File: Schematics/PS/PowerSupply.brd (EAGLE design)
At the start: 157.5 x 127 mm, 79 parts, among them IC1 LM317MABDT, IC2 LM337, T1 IRFP240, T2 IRFP240

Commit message: updates to PS
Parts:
- moved C3 144.5 mm to (144.1, 12.6)
- moved D11 94.0 mm to (170.2, 17.6)
- moved D18 68.4 mm to (126.6, 12.2)
- moved C21 58.1 mm to (144.8, 35.0), turned to 270 degrees
- moved C24 55.6 mm to (163.3, 56.4)
- moved IC2 48.8 mm to (152.4, 24.5)
- moved C18 47.1 mm to (137.9, 37.9), turned to 270 degrees
- moved C22 46.6 mm to (152.9, 34.8)
- moved R12 45.6 mm to (153.5, 55.8), turned to 90 degrees
- moved C8 44.0 mm to (79.9, 13.5)
- moved R21 41.5 mm to (187.2, 51.3)
- moved IC1 35.6 mm to (137.8, 23.6), turned to 180 degrees
- moved C20 29.6 mm to (148.7, 41.5), turned to 180 degrees
- moved D14 25.1 mm to (137.8, 46.1), turned to 90 degrees
- moved D17 24.8 mm to (153.2, 19.3)
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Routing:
- net MUTE: track 4.44 -> 62.0 mm
- net V+: track 128.5 -> 91.1 mm
- net N$10: track 15.6 -> 48.6 mm
- net SGND: track 54.5 -> 84.0 mm
- net VAC+15: track 0.00 -> 23.3 mm
- net VAC-15: track 0.00 -> 17.8 mm
- net N$1: track 17.4 -> 23.2 mm
- net N$21: track 9.27 -> 14.7 mm
- net VAC+40: track 50.0 -> 55.1 mm
- net VAC-40: track 34.9 -> 39.8 mm
- net V-15UN: track 0.00 -> 3.07 mm
- net V15UN: track 0.00 -> 2.74 mm
- net N$9: track 32.1 -> 34.8 mm
- net N$22: track 91.1 -> 93.7 mm
- net VCC: track 119.0 -> 120.2 mm
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
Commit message: finished powersuply :) updated parts on hand
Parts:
- C28: device rcl:C102-064X133 -> rcl:C0805K
- moved R21 125.2 mm to (62.9, 35.7), turned to 180 degrees
- moved C23 118.8 mm to (76.2, 26.6), turned to 90 degrees
- moved R22 118.5 mm to (61.3, 31.0), turned to 90 degrees
- moved C24 109.8 mm to (57.1, 28.3), turned to 90 degrees
- moved D17 89.6 mm to (64.7, 33.8), turned to 270 degrees
- moved D12 80.6 mm to (147.6, 20.9), turned to 90 degrees
- moved IC2 79.8 mm to (73.2, 33.8), turned to 270 degrees
- moved C3 76.0 mm to (69.1, 24.6), turned to 90 degrees
- moved R19 73.7 mm to (147.0, 19.7)
- moved C8 71.7 mm to (29.8, 64.9), turned to 180 degrees
- moved C6 69.6 mm to (143.1, 22.4), turned to 180 degrees
- moved C14 67.3 mm to (152.0, 20.8)
- moved D18 61.3 mm to (67.6, 29.0)
- moved C16 40.6 mm to (150.4, 29.0), turned to 90 degrees
- moved R18 32.8 mm to (16.2, 60.4), turned to 90 degrees
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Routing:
- net V15+: track 0.00 -> 130.5 mm
- net VEE: track 44.8 -> 169.4 mm
- net MUTE: track 62.0 -> 182.6 mm
- net V-15UN: track 3.07 -> 122.5 mm
- net VCC: track 120.2 -> 197.2 mm
- net V15-: track 0.00 -> 36.2 mm
- net V15UN: track 2.74 -> 36.7 mm
- net N$3: track 0.00 -> 18.9 mm
- net GND: track 11.2 -> 28.7 mm, vias 0 -> 1
- net N$26: track 0.00 -> 13.7 mm
- net EGND: track 27.0 -> 31.1 mm
- net N$25: track 0.00 -> 3.82 mm
- net N$8: track 0.00 -> 2.88 mm
- net VAC+40: track 55.1 -> 56.4 mm
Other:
- board size 157.5 x 127 mm -> 157.5 x 109.9 mm

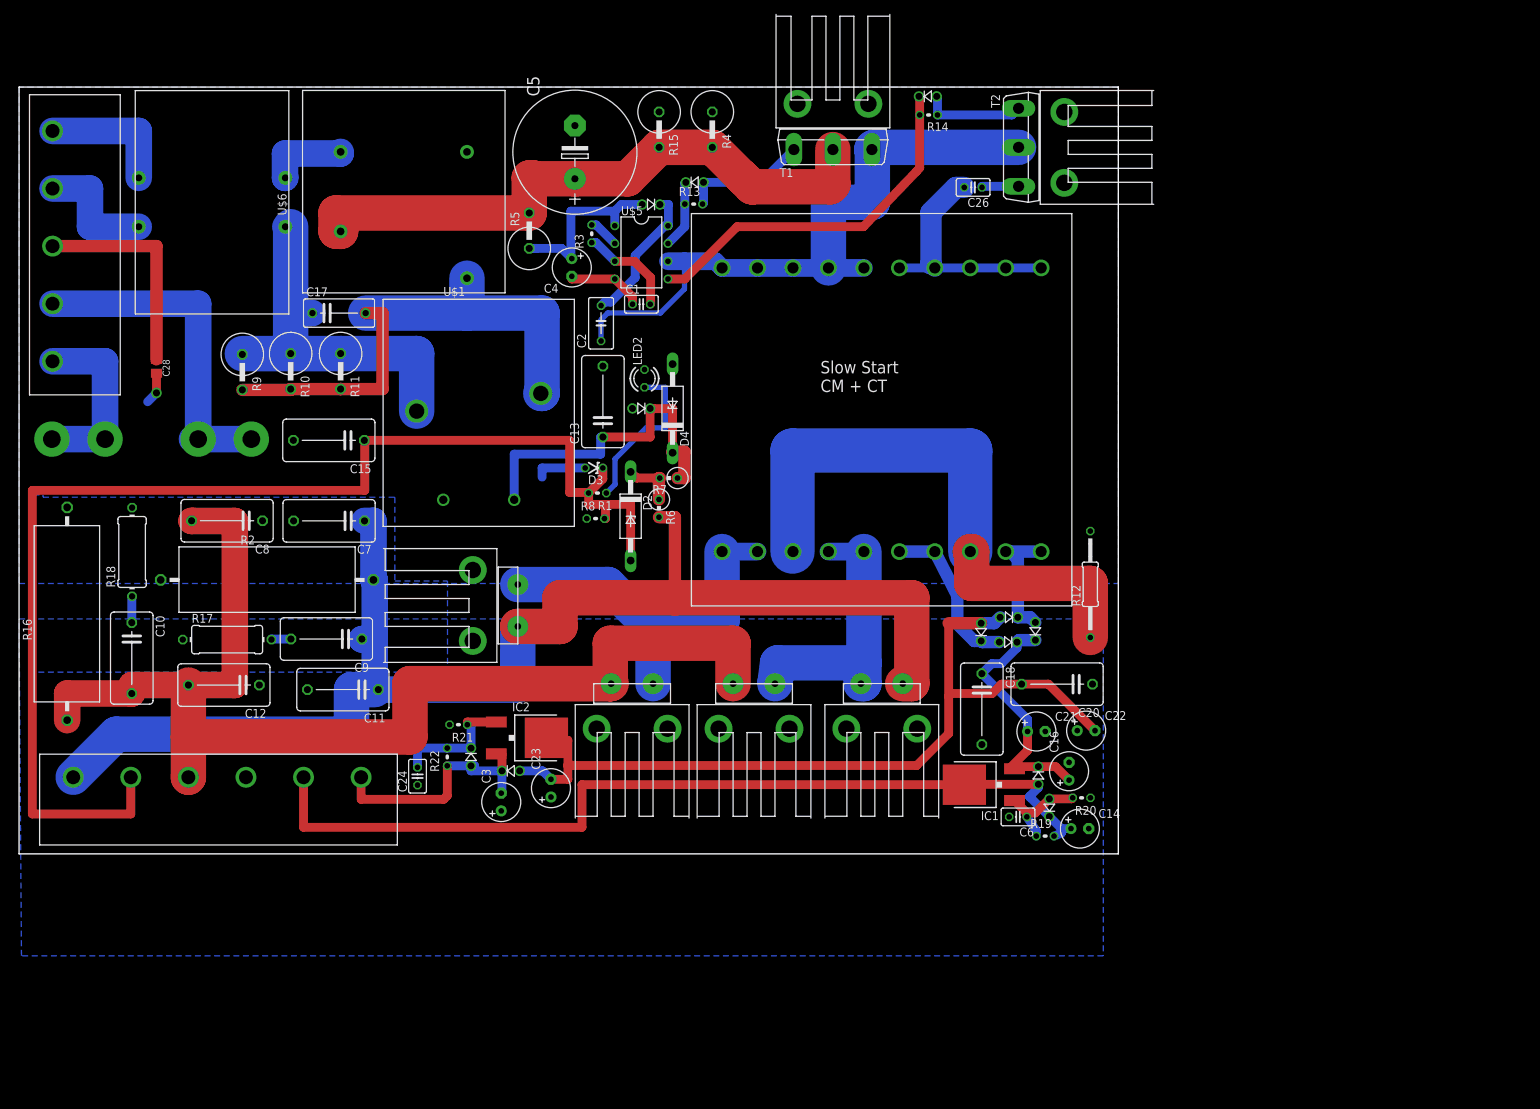
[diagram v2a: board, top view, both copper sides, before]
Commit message: fixed PS layout (changed rectifier footprint)
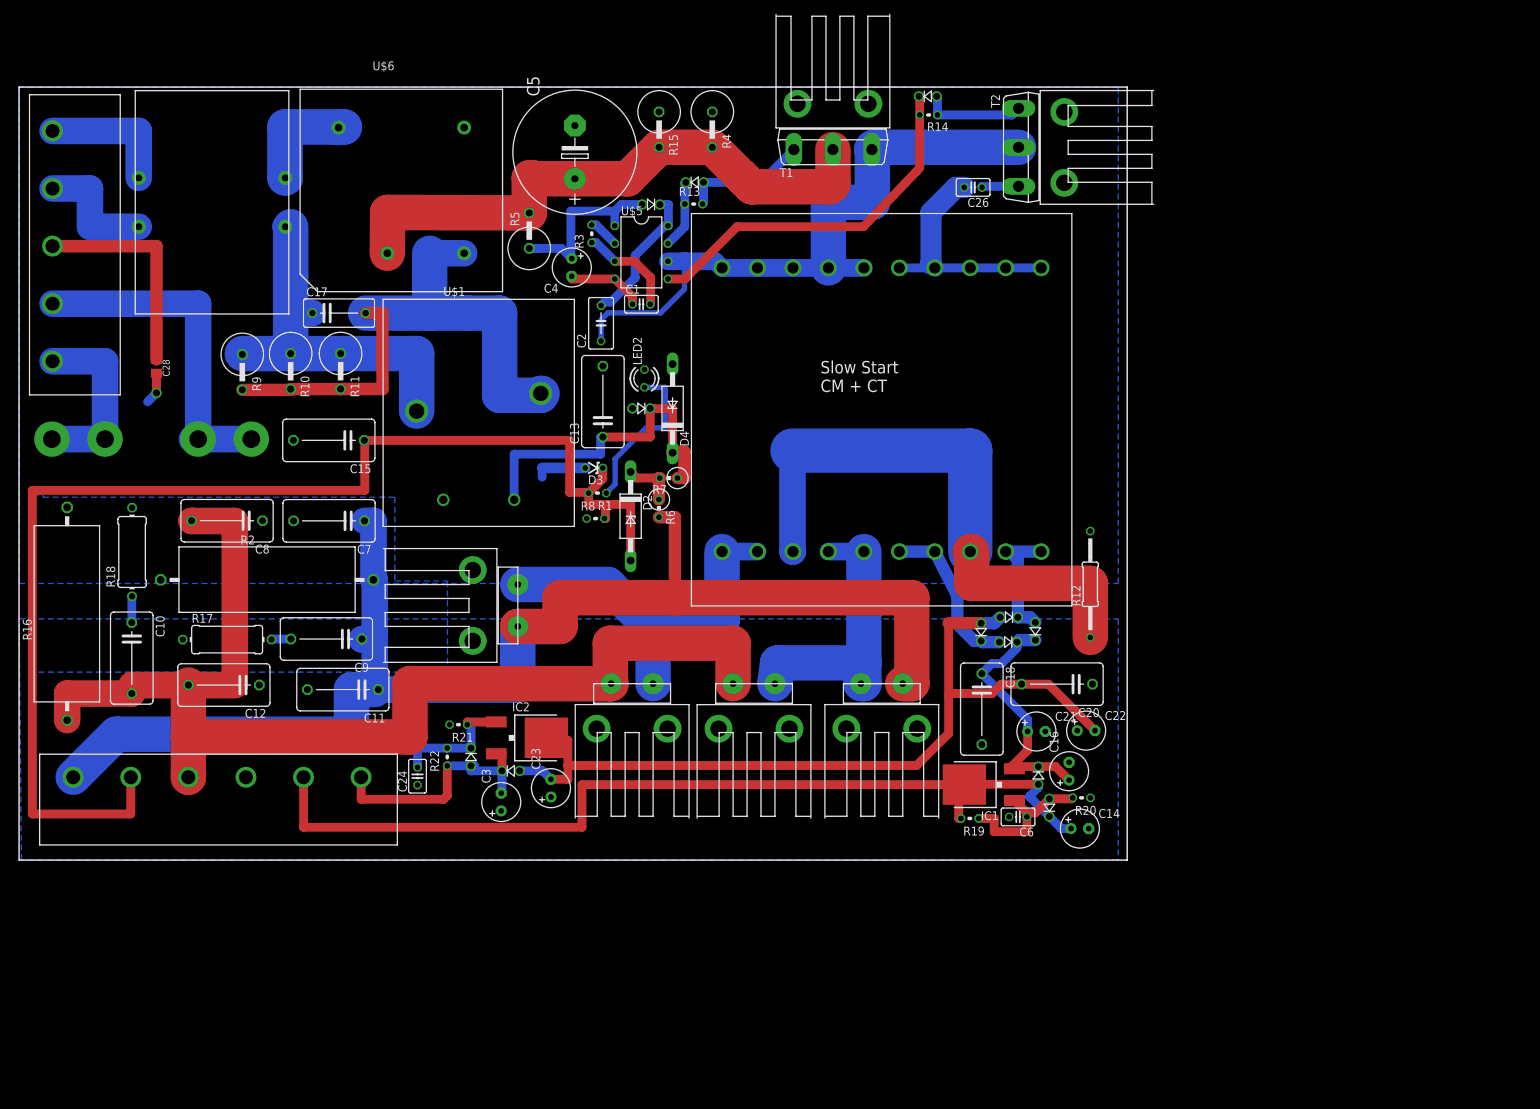
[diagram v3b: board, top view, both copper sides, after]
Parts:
- moved R19 11.1 mm to (136.2, 22.2), turned to 180 degrees
- moved U$6 8.03 mm to (52.8, 103.2), turned to 0 degrees
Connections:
- net GND: now also U$6.-; no longer U$6.V-
- net V+: now also U$6.+; no longer U$6.V+
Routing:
- net N$18: track 75.5 -> 84.4 mm
- net N$26: track 13.7 -> 21.5 mm
- net N$4: track 11.7 -> 16.7 mm
- net V+: track 91.1 -> 86.3 mm
- net V15+: track 130.5 -> 133.9 mm
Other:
- board size 157.5 x 109.9 mm -> 158.8 x 110.7 mm
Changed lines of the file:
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@@
 <setting verticaltext="up"/>
 </settings>
-<grid distance="0.025" unitdist="inch" unit="inch" style="lines" multiple="1" display="yes" altdistance="0.025" altunitdist="inch" altunit="inch"/>
+<grid distance="0.003125" unitdist="mic" unit="inch" style="lines" multiple="1" display="yes" altdistance="0.025" altunitdist="inch" altunit="inch"/>
 <layers>
 <layer number="1" name="Top" color="4" fill="1" visible="yes" active="yes"/>
@@
 <board>
 <plain>
-<wire x1="0" y1="17.145" x2="157.48" y2="17.145" width="0" layer="20"/>
-<wire x1="157.48" y1="17.145" x2="157.48" y2="127" width="0" layer="20"/>
-<wire x1="157.48" y1="127" x2="0" y2="127" width="0" layer="20"/>
-<wire x1="0" y1="127" x2="0" y2="17.145" width="0" layer="20"/>
+<wire x1="0" y1="16.256" x2="158.75" y2="16.256" width="0" layer="20"/>
+<wire x1="158.75" y1="16.256" x2="158.75" y2="127" width="0" layer="20"/>
+<wire x1="158.75" y1="127" x2="0" y2="127" width="0" layer="20"/>
+<wire x1="0" y1="127" x2="0" y2="16.256" width="0" layer="20"/>
 <text x="114.808" y="83.312" size="1.778" layer="21" font="vector">Slow Start
 CM + CT</text>
@@
 <element name="R3" library="rcl" package="0204V" value="" x="82.042" y="105.9815" rot="R90"/>
 <element name="C1" library="resistor" package="C025-025X050" value="" x="89.154" y="95.885"/>
-<element name="U$6" library="Amplifier_Parts" package="GBPC3510W" value="GBPC3510W" x="50.038" y="110.744" rot="R90"/>
+<element name="U$6" library="Amplifier_Parts" package="GBPC3510W" value="GBPC3510W" x="52.76455625" y="103.188453125"/>
 <element name="C4" library="rcl" package="E2,5-6" value="100uF" x="79.1845" y="101.1555" smashed="yes" rot="R270">
 <attribute name="NAME" x="75.184" y="97.536" size="1.27" layer="25" ratio="10"/>
@@
 <element name="D11" library="Amplifier_Parts" package="1N4004" value="1N4004" x="146.0256875" y="31.1901875" rot="R270"/>
 <element name="D12" library="Amplifier_Parts" package="1N4004" value="1N4004" x="147.60016875" y="20.948165625" rot="R90"/>
-<element name="R19" library="rcl" package="0204V" value="10k" x="147.000615625" y="19.693478125"/>
+<element name="R19" library="rcl" package="0204V" value="10k" x="136.209384375" y="22.216521875" rot="R180"/>
 <element name="R20" library="rcl" package="0204V" value="10k" x="152.216559375" y="25.17390625" rot="R180"/>
 <element name="C6" library="resistor" package="C025-025X050" value="10uF" x="143.111490625" y="22.441559375" rot="R180"/>
@@
 <contactref element="C26" pad="1"/>
 <contactref element="C28" pad="2"/>
-<contactref element="U$6" pad="V-"/>
+<contactref element="U$6" pad="-"/>
 <contactref element="C5" pad="-"/>
 <contactref element="R15" pad="1"/>
@@
 <wire x1="143.1925" y1="112.776" x2="137.9474" y2="112.776" width="1.27" layer="16"/>
 <wire x1="137.9474" y1="112.776" x2="137.9474" y2="112.6236" width="1.27" layer="16"/>
-<wire x1="81.0934375" y1="72.432103125" x2="74.93" y2="72.432103125" width="1.27" layer="16"/>
+<wire x1="81.0934375" y1="72.432103125" x2="74.93" y2="72.432103125" width="1.524" layer="16"/>
 <wire x1="74.93" y1="72.432103125" x2="74.93" y2="71.12" width="1.27" layer="16"/>
 </signal>
@@
 <signal name="V+">
 <contactref element="T1" pad="D"/>
-<contactref element="U$6" pad="V+"/>
+<contactref element="U$6" pad="+"/>
 <contactref element="C5" pad="+"/>
 <contactref element="R15" pad="2"/>
@@
 <wire x1="73.66" y1="113.9825" x2="73.0885" y2="113.9825" width="5.08" layer="1"/>
 <wire x1="73.0885" y1="113.9825" x2="73.0885" y2="108.966" width="5.08" layer="1"/>
-<wire x1="73.0885" y1="108.966" x2="45.4025" y2="108.966" width="5.08" layer="1"/>
-<wire x1="45.4025" y1="108.966" x2="45.4025" y2="106.3625" width="5.08" layer="1"/>
-<wire x1="45.4025" y1="106.3625" x2="46.068" y2="106.3625" width="5.08" layer="1"/>
-<wire x1="46.068" y1="106.3625" x2="46.068" y2="106.314" width="5.08" layer="1"/>
+<wire x1="73.0885" y1="108.966" x2="52.7991" y2="109.0407" width="5.08" layer="1"/>
+<wire x1="52.7991" y1="109.0407" x2="52.76455625" y2="103.188453125" width="5.08" layer="1"/>
 </signal>
 <signal name="N$17">
@@
 <contactref element="C17" pad="2"/>
 <contactref element="U$6" pad="AC2"/>
-<wire x1="49.6514" y1="94.61909375" x2="64.168" y2="94.61909375" width="5.08" layer="16"/>
-<wire x1="64.168" y1="94.61909375" x2="64.168" y2="99.614" width="5.08" layer="16"/>
+<wire x1="49.6514" y1="94.61909375" x2="58.8267" y2="94.61909375" width="5.08" layer="16"/>
+<wire x1="58.8267" y1="94.61909375" x2="64.168" y2="94.61909375" width="5.08" layer="16"/>
 <wire x1="74.741696875" y1="83.110078125" x2="74.93" y2="83.110078125" width="5.08" layer="16"/>
-<wire x1="74.93" y1="83.110078125" x2="74.93" y2="94.615" width="5.08" layer="16"/>
-<wire x1="74.93" y1="94.615" x2="64.168" y2="94.615" width="5.08" layer="16"/>
 <wire x1="64.168" y1="94.615" x2="64.168" y2="94.61909375" width="5.08" layer="16"/>
 <wire x1="31.983978125" y1="83.615234375" x2="38.907159375" y2="83.615234375" width="1.778" layer="1"/>
@@
 <wire x1="52.07" y1="83.741671875" x2="52.07" y2="94.61909375" width="1.778" layer="1"/>
 <wire x1="52.07" y1="94.61909375" x2="49.6514" y2="94.61909375" width="1.778" layer="1"/>
+<wire x1="63.76455625" y1="103.188453125" x2="58.8267" y2="103.188453125" width="3.81" layer="16"/>
+<wire x1="58.8267" y1="103.188453125" x2="58.8267" y2="94.61909375" width="5.08" layer="16"/>
+<wire x1="64.168" y1="94.615" x2="68.843828125" y2="94.615" width="5.08" layer="16"/>
+<wire x1="68.843828125" y1="94.615" x2="68.843828125" y2="82.834596875" width="5.08" layer="16"/>
+<wire x1="68.843828125" y1="82.834596875" x2="74.741696875" y2="82.834596875" width="5.08" layer="16"/>
+<wire x1="74.741696875" y1="82.834596875" x2="74.741696875" y2="83.110078125" width="5.08" layer="16"/>
 </signal>
 <signal name="N$1">
@@
 <contactref element="U$3" pad="P$3"/>
 <contactref element="C14" pad="-"/>
-<wire x1="110.871" y1="60.452" x2="110.8075" y2="60.452" width="5.08" layer="16"/>
-<wire x1="110.8075" y1="60.452" x2="110.8075" y2="74.93" width="6.35" layer="16"/>
+<wire x1="110.871" y1="60.452" x2="110.8075" y2="60.452" width="3.81" layer="16"/>
+<wire x1="110.8075" y1="60.452" x2="110.8075" y2="74.93" width="3.81" layer="16"/>
 <wire x1="110.8075" y1="74.93" x2="136.271" y2="74.93" width="6.35" layer="16"/>
 <wire x1="136.271" y1="74.93" x2="136.271" y2="60.452" width="6.35" layer="16"/>
 <contactref element="C3" pad="+"/>
-<polygon width="0.254" layer="16" isolate="0.762">
+<polygon width="0.254" layer="16" isolate="1.27">
 <vertex x="0" y="50.8"/>
-<vertex x="155.3337" y="50.8"/>
-<vertex x="155.3337" y="2.54"/>
-<vertex x="0.3429" y="2.54"/>
+<vertex x="157.48" y="50.8"/>
+<vertex x="157.48" y="16.256"/>
+<vertex x="0.3429" y="16.256"/>
 </polygon>
 <polygon width="0.254" layer="16" isolate="2.032">
@@
 <wire x1="147.60016875" y1="22.488165625" x2="149.320571875" y2="20.7677625" width="1.27" layer="16"/>
 <wire x1="149.320571875" y1="20.7677625" x2="150.700871875" y2="20.7677625" width="1.27" layer="16"/>
-<wire x1="148.270615625" y1="19.693478125" x2="149.320571875" y2="20.108434375" width="1.27" layer="16"/>
-<wire x1="149.320571875" y1="20.108434375" x2="149.320571875" y2="20.7677625" width="1.27" layer="16"/>
-<wire x1="135.429659375" y1="27.06104375" x2="80.645" y2="27.06104375" width="1.27" layer="1"/>
+<wire x1="135.429659375" y1="27.06104375" x2="134.62" y2="27.06104375" width="1.27" layer="1"/>
+<wire x1="134.62" y1="27.06104375" x2="80.645" y2="27.06104375" width="1.27" layer="1"/>
 <wire x1="80.645" y1="27.06104375" x2="80.645" y2="20.955" width="1.27" layer="1"/>
 <wire x1="80.645" y1="20.955" x2="40.754225" y2="20.955" width="1.27" layer="1"/>
@@
 <wire x1="144.78" y1="25.4" x2="144.78" y2="25.308334375" width="1.27" layer="16"/>
 <wire x1="144.78" y1="25.308334375" x2="147.60016875" y2="22.488165625" width="1.27" layer="16"/>
+<wire x1="134.939384375" y1="22.216521875" x2="134.62" y2="22.216521875" width="1.27" layer="1"/>
+<wire x1="134.62" y1="22.216521875" x2="134.62" y2="27.06104375" width="1.27" layer="1"/>
 </signal>
 <signal name="N$26">
@@
 <wire x1="150.946559375" y1="25.17390625" x2="150.80081875" y2="25.028165625" width="1.27" layer="1"/>
 <wire x1="150.80081875" y1="25.028165625" x2="147.60016875" y2="25.028165625" width="1.27" layer="1"/>
-<wire x1="144.381490625" y1="22.441559375" x2="145.730615625" y2="20.457434375" width="1.27" layer="16"/>
-<wire x1="145.730615625" y1="20.457434375" x2="145.730615625" y2="19.693478125" width="1.27" layer="16"/>
+<wire x1="137.479384375" y1="22.216521875" x2="139.7" y2="22.216521875" width="1.27" layer="1"/>
+<wire x1="139.7" y1="22.216521875" x2="139.7" y2="20.32" width="1.27" layer="1"/>
+<wire x1="139.7" y1="20.32" x2="144.381490625" y2="20.32" width="1.27" layer="1"/>
+<wire x1="144.381490625" y1="20.32" x2="144.381490625" y2="22.441559375" width="1.27" layer="1"/>
 </signal>
 <signal name="V15UN">
@@
 <contactref element="U$6" pad="AC1"/>
 <contactref element="L2" pad="PASS2"/>
-<wire x1="38.145" y1="113.99" x2="38.1" y2="113.99" width="3.81" layer="16"/>
-<wire x1="38.1" y1="113.99" x2="38.1" y2="117.475" width="3.81" layer="16"/>
-<wire x1="38.1" y1="117.475" x2="46.068" y2="117.475" width="3.81" layer="16"/>
-<wire x1="46.068" y1="117.475" x2="46.068" y2="117.714" width="3.81" layer="16"/>
+<wire x1="38.145" y1="113.99" x2="38.1" y2="113.99" width="5.08" layer="16"/>
+<wire x1="38.1" y1="113.99" x2="38.1" y2="121.285" width="5.08" layer="16"/>
+<wire x1="38.1" y1="121.285" x2="46.594" y2="121.285" width="5.08" layer="16"/>
+<wire x1="46.594" y1="121.285" x2="45.76455625" y2="121.188453125" width="5.08" layer="16"/>
 </signal>
 <signal name="N$5">

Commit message: updates to PS layout
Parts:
- moved C23 4.92 mm to (71.8, 24.4)
- moved C3 4.19 mm to (64.9, 24.6)
- moved IC2 2.11 mm to (71.1, 33.7)
- moved D8 1.61 mm to (86.2, 41.5)
- moved R21 1.50 mm to (61.5, 35.8)
- moved D17 1.39 mm to (63.4, 33.7)
- moved R22 0.72 mm to (60.6, 31.1)
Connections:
- net N$15 renamed LINE
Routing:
- net V15-: track 36.2 -> 43.8 mm
- net N$3: track 18.9 -> 21.1 mm
- net V-15UN: track 122.5 -> 124.4 mm
- net VAC+40: track 56.4 -> 57.7 mm
